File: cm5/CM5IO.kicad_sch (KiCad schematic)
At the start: 11 parts, among them J2 B2B-XH-A_LF__SN_

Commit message: Ordered v2 PCB
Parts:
- J2: value B2B-XH-A_LF__SN_ -> 1x4; symbol dk_Rectangular-Connectors-Headers-Male-Pins:B2B-XH-A_LF__SN_ -> Connector_Generic:Conn_01x04
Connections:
- net +5v: now also J2.1 (Pin_1), J2.4 (Pin_4); no longer J2.2
- net GND: now also J2.2 (Pin_2), J2.3 (Pin_3); no longer J2.1
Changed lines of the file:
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@@
+	)
+	(junction
+		(at 44.45 82.55)
+		(diameter 0)
+		(color 0 0 0 0)
 	)
 	(junction
@@
 		(color 0 0 0 0)
 	)
+	(junction
+		(at 40.64 85.09)
+		(diameter 0)
+		(color 0 0 0 0)
+	)
 	(wire
 		(pts
@@
 	(wire
 		(pts
-			(xy 238.76 86.36) (xy 238.76 161.29)
-		)
-		(stroke
-			(width 0)
-			(type default)
-		)
-	)
-	(wire
-		(pts
-			(xy 153.67 168.91) (xy 232.41 168.91)
-		)
-		(stroke
-			(width 0)
-			(type default)
-		)
-	)
-	(wire
-		(pts
 			(xy 115.57 76.2) (xy 129.54 76.2)
 		)
@@
 	(wire
 		(pts
-			(xy 153.67 168.91) (xy 153.67 157.48)
-		)
-		(stroke
-			(width 0)
-			(type default)
-		)
-	)
-	(wire
-		(pts
-			(xy 50.8 78.74) (xy 50.8 82.55)
-		)
-		(stroke
-			(width 0)
-			(type default)
-		)
-	)
-	(wire
-		(pts
 			(xy 186.69 72.39) (xy 200.66 72.39)
 		)
@@
 	(wire
 		(pts
+			(xy 45.72 85.09) (xy 40.64 85.09)
+		)
+		(stroke
+			(width 0)
+			(type default)
+		)
+	)
+	(wire
+		(pts
 			(xy 204.47 48.26) (xy 214.63 48.26)
 		)
@@
 	(wire
 		(pts
-			(xy 149.86 170.18) (xy 241.3 170.18)
-		)
-		(stroke
-			(width 0)
-			(type default)
-		)
-	)
-	(wire
-		(pts
 			(xy 228.6 166.37) (xy 157.48 166.37)
 		)
@@
 	(wire
 		(pts
-			(xy 53.34 82.55) (xy 53.34 78.74)
+			(xy 44.45 90.17) (xy 45.72 90.17)
 		)
 		(stroke
@@
 	(wire
 		(pts
-			(xy 149.86 157.48) (xy 149.86 170.18)
-		)
-		(stroke
-			(width 0)
-			(type default)
-		)
-	)
-	(wire
-		(pts
 			(xy 162.56 96.52) (xy 162.56 111.76)
 		)
@@
 	(wire
 		(pts
+			(xy 40.64 85.09) (xy 33.02 85.09)
+		)
+		(stroke
+			(width 0)
+			(type default)
+		)
+	)
+	(wire
+		(pts
 			(xy 92.71 101.6) (xy 92.71 104.14)
 		)
@@
 	(wire
 		(pts
+			(xy 44.45 80.01) (xy 44.45 82.55)
+		)
+		(stroke
+			(width 0)
+			(type default)
+		)
+	)
+	(wire
+		(pts
 			(xy 200.66 72.39) (xy 200.66 62.23)
 		)
@@
 	(wire
 		(pts
+			(xy 40.64 87.63) (xy 40.64 85.09)
+		)
+		(stroke
+			(width 0)
+			(type default)
+		)
+	)
+	(wire
+		(pts
 			(xy 129.54 50.8) (xy 120.65 50.8)
 		)
@@
 	(wire
 		(pts
-			(xy 175.26 161.29) (xy 175.26 157.48)
-		)
-		(stroke
-			(width 0)
-			(type default)
-		)
-	)
-	(wire
-		(pts
-			(xy 236.22 160.02) (xy 236.22 86.36)
+			(xy 44.45 82.55) (xy 44.45 90.17)
+		)
+		(stroke
+			(width 0)
+			(type default)
+		)
+	)
+	(wire
+		(pts
+			(xy 45.72 87.63) (xy 40.64 87.63)
 		)
 		(stroke
@@
 	(wire
 		(pts
-			(xy 179.07 157.48) (xy 179.07 160.02)
+			(xy 45.72 82.55) (xy 44.45 82.55)
 		)
 		(stroke
@@
 	(wire
 		(pts
-			(xy 232.41 86.36) (xy 232.41 168.91)
-		)
-		(stroke
-			(width 0)
-			(type default)
-		)
-	)
-	(wire
-		(pts
 			(xy 204.47 22.86) (xy 204.47 48.26)
 		)
@@
 	(wire
 		(pts
-			(xy 179.07 160.02) (xy 236.22 160.02)
-		)
-		(stroke
-			(width 0)
-			(type default)
-		)
-	)
-	(wire
-		(pts
 			(xy 115.57 72.39) (xy 129.54 72.39)
 		)
@@
 		(pts
 			(xy 123.19 22.86) (xy 204.47 22.86)
-		)
-		(stroke
-			(width 0)
-			(type default)
-		)
-	)
-	(wire
-		(pts
-			(xy 241.3 170.18) (xy 241.3 86.36)
-		)
-		(stroke
-			(width 0)
-			(type default)
-		)
-	)
-	(wire
-		(pts
-			(xy 238.76 161.29) (xy 175.26 161.29)
 		)
 		(stroke
@@
 	)
 	(label "+5v"
-		(at 53.34 78.74 0)
+		(at 44.45 80.01 0)
 		(effects
 			(font
@@
 	)
 	(symbol
-		(lib_id "dk_Rectangular-Connectors-Headers-Male-Pins:B2B-XH-A_LF__SN_")
+		(lib_id "Connector_Generic:Conn_01x04")
 		(at 50.8 85.09 0)
 		(unit 1)
@@
 		(fields_autoplaced yes)
 		(property "Reference" "J2"
-			(at 55.88 85.0899 0)
-			(effects
-				(font
-					(size 1.27 1.27)
-				)
-				(justify left)
-			)
-		)
-		(property "Value" "B2B-XH-A_LF__SN_"
-			(at 55.88 87.6299 0)
+			(at 53.34 85.0899 0)
+			(effects
+				(font
+					(size 1.27 1.27)
+				)
+				(justify left)
+			)
+		)
+		(property "Value" "1x4"
+			(at 53.34 87.6299 0)
 			(effects
 				(font
@@
 		)
 		(property "Footprint" "digikey-footprints:PinHeader_1x2_P2.5mm_Drill1.1mm"
-			(at 55.88 80.01 0)
-			(effects
-				(font
-					(size 1.524 1.524)
-				)
-				(justify left)
-				(hide yes)
-			)
-		)
-		(property "Datasheet" "http://www.jst-mfg.com/product/pdf/eng/eXH.pdf"
-			(at 55.88 77.47 0)
-			(effects
-				(font
-					(size 1.524 1.524)
-				)
-				(justify left)
-				(hide yes)
-			)
-		)
-		(property "Description" "CONN HEADER VERT 2POS 2.5MM"
+			(at 50.8 85.09 0)
+			(effects
+				(font
+					(size 1.27 1.27)
+				)
+				(hide yes)
+			)
+		)
+		(property "Datasheet" "~"
+			(at 50.8 85.09 0)
+			(effects
+				(font
+					(size 1.27 1.27)
+				)
+				(hide yes)
+			)
+		)
+		(property "Description" "Generic connector, single row, 01x04, script generated (kicad-library-utils/schlib/autogen/connector/)"
 			(at 50.8 85.09 0)
 			(effects
@@
 		)
 		(pin "1"
+		)
+		(pin "3"
+		)
+		(pin "4"
 		)
 		(instances
@@
 	(symbol
 		(lib_id "power:GND")
-		(at 50.8 78.74 180)
+		(at 33.02 85.09 180)
 		(unit 1)
 		(exclude_from_sim no)
@@
 		(dnp no)
 		(property "Reference" "#PWR063"
-			(at 50.8 72.39 0)
+			(at 33.02 78.74 0)
 			(effects
 				(font
@@
 		)
 		(property "Value" "GND"
-			(at 50.673 74.3458 0)
+			(at 32.893 80.6958 0)
 			(effects
 				(font
@@
 		)
 		(property "Footprint" ""
-			(at 50.8 78.74 0)
+			(at 33.02 85.09 0)
 			(effects
 				(font
@@
 		)
 		(property "Datasheet" ""
-			(at 50.8 78.74 0)
+			(at 33.02 85.09 0)
 			(effects
 				(font
@@
 		)
 		(property "Description" "Power symbol creates a global label with name \"GND\" , ground"
-			(at 50.8 78.74 0)
-			(effects
-				(font
+			(at 33.02 85.09 0)
+			(effects
+				(font

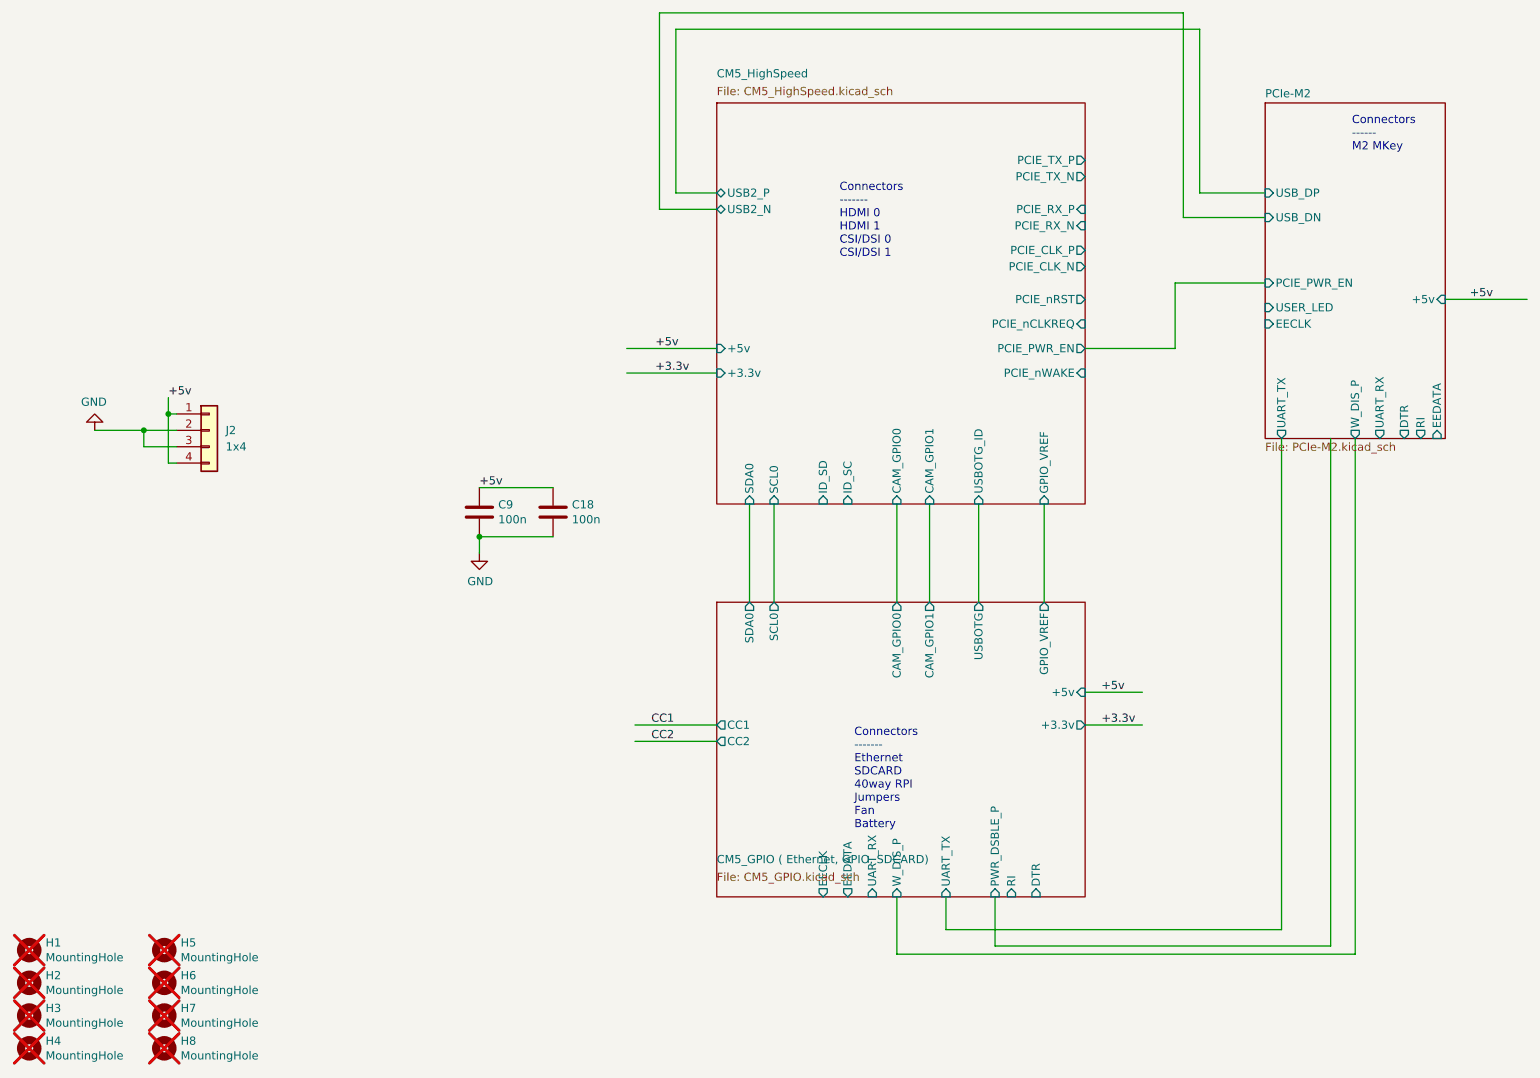
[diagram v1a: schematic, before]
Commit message: PCM1863 switchover (#5)
* Oops, basically brand new ADC design using a new chip

* Working PCB and working driver, sort of

* --amend
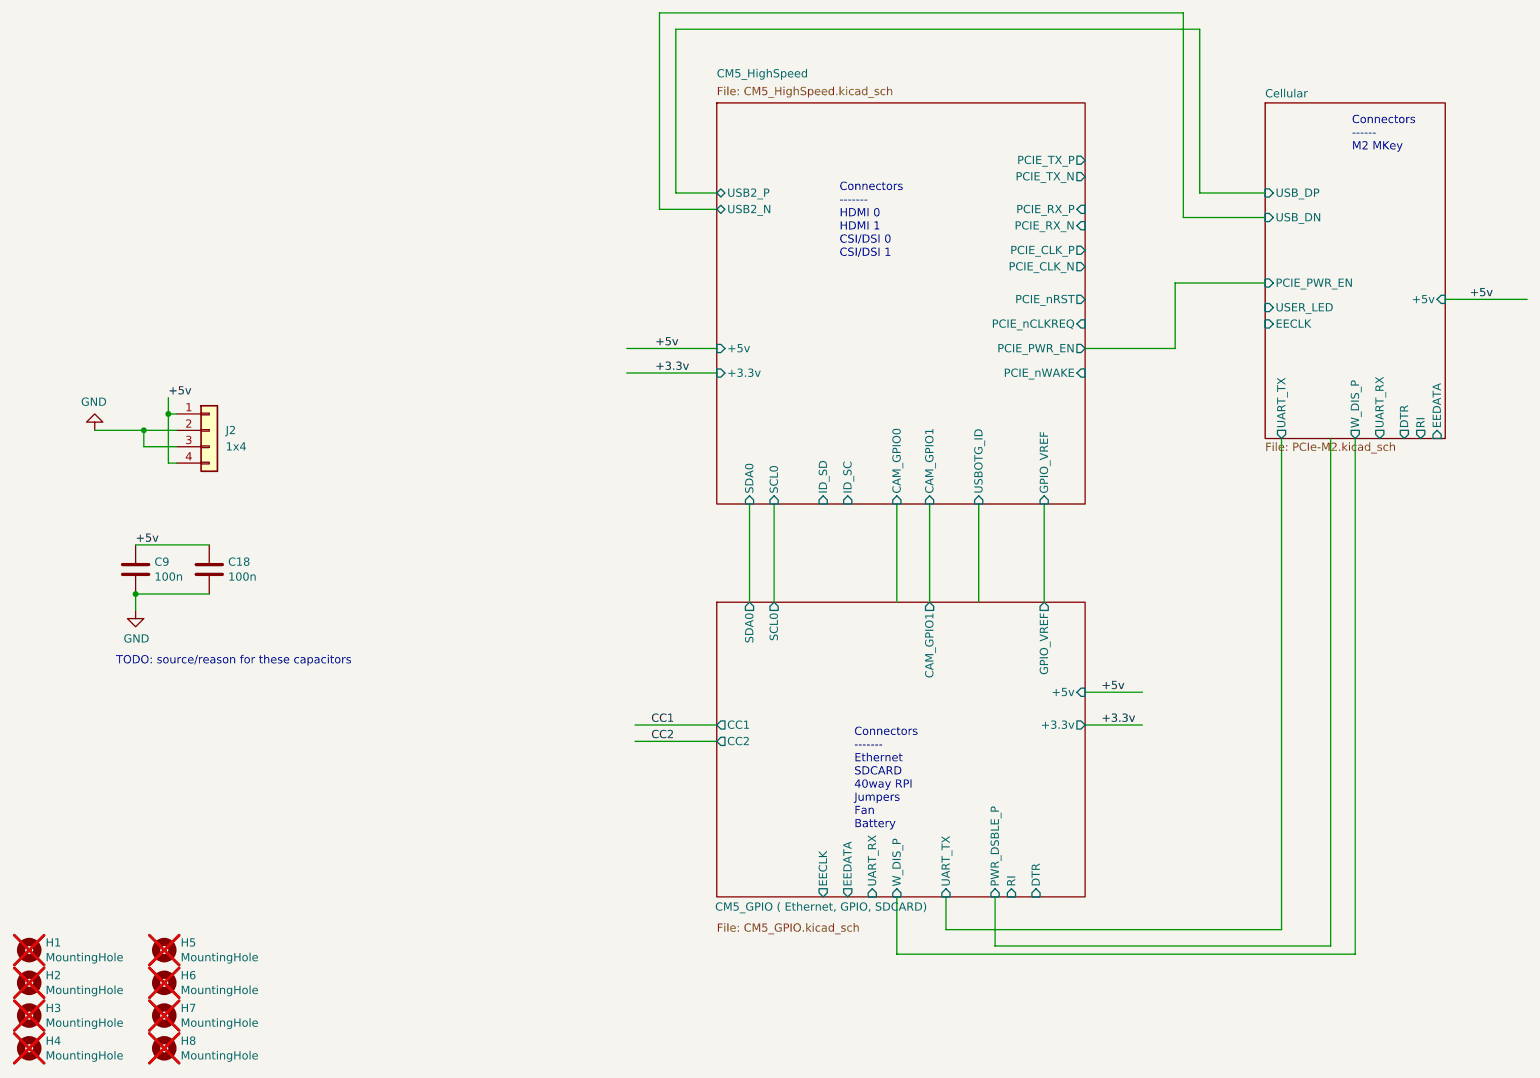
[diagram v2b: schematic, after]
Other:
- sheet PCIe-M2 renamed Cellular
- sheet CM5_GPIO ( Ethernet, GPIO, SDCARD) ports: added none; removed CAM_GPIO0, USBOTG
- note added: "TODO: source/reason for these capacitors"
- moved on the sheet: C18, C9
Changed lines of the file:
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@@
+		)
+	)
+	(text "TODO: source/reason for these capacitors"
+		(exclude_from_sim no)
+		(at 54.61 120.904 0)
+		(effects
+			(font
+				(size 1.27 1.27)
+			)
 		)
 	)
@@
 	)
 	(junction
-		(at 92.71 101.6)
+		(at 39.37 110.49)
 		(diameter 0)
 		(color 0 0 0 0)
@@
 	(wire
 		(pts
-			(xy 92.71 101.6) (xy 104.14 101.6)
+			(xy 39.37 110.49) (xy 50.8 110.49)
 		)
 		(stroke
@@
 	(wire
 		(pts
-			(xy 92.71 101.6) (xy 92.71 104.14)
+			(xy 39.37 110.49) (xy 39.37 113.03)
 		)
 		(stroke
@@
 	(wire
 		(pts
-			(xy 92.71 93.98) (xy 104.14 93.98)
+			(xy 39.37 102.87) (xy 50.8 102.87)
 		)
 		(stroke
@@
 	)
 	(label "+5v"
-		(at 92.71 93.98 0)
+		(at 39.37 102.87 0)
 		(effects
 			(font
@@
 	(symbol
 		(lib_id "Device:C")
-		(at 104.14 97.79 0)
+		(at 50.8 106.68 0)
 		(unit 1)
 		(exclude_from_sim no)
@@
 		(dnp no)
 		(property "Reference" "C18"
-			(at 107.061 96.6216 0)
+			(at 53.721 105.5116 0)
 			(effects
 				(font
@@
 		)
 		(property "Value" "100n"
-			(at 107.061 98.933 0)
+			(at 53.721 107.823 0)
 			(effects
 				(font
@@
 		)
 		(property "Footprint" "Capacitor_SMD:C_0402_1005Metric"
-			(at 105.1052 101.6 0)
+			(at 51.7652 110.49 0)
 			(effects
 				(font
@@
 		)
 		(property "Datasheet" "https://search.murata.co.jp/Ceramy/image/img/A01X/G101/ENG/GRM155R71C104KA88-01.pdf"
-			(at 104.14 97.79 0)
+			(at 50.8 106.68 0)
 			(effects
 				(font
@@
 		)
 		(property "Description" ""
-			(at 104.14 97.79 0)
+			(at 50.8 106.68 0)
 			(effects
 				(font
@@
 		)
 		(property "Field4" "Farnell"
-			(at 104.14 97.79 0)
+			(at 50.8 106.68 0)
 			(effects
 				(font
@@
 		)
 		(property "Field5" "2611911"
-			(at 104.14 97.79 0)
+			(at 50.8 106.68 0)
 			(effects
 				(font
@@
 		)
 		(property "Field6" "RM EMK105 B7104KV-F"
-			(at 104.14 97.79 0)
+			(at 50.8 106.68 0)
 			(effects
 				(font
@@
 		)
 		(property "Field7" "TAIYO YUDEN EUROPE GMBH"
-			(at 104.14 97.79 0)
+			(at 50.8 106.68 0)
 			(effects
 				(font
@@
 		)
 		(property "Field8" "110091611"
-			(at 104.14 97.79 0)
+			(at 50.8 106.68 0)
 			(effects
 				(font
@@
 		)
 		(property "Part Description" "	0.1uF 10% 16V Ceramic Capacitor X7R 0402 (1005 Metric)"
-			(at 104.14 97.79 0)
+			(at 50.8 106.68 0)
 			(effects
 				(font
@@
 		)
 		(property "LCSC" "C327024"
-			(at 104.14 97.79 0)
+			(at 50.8 106.68 0)
 			(effects
 				(font
@@
 	(symbol
 		(lib_id "Device:C")
-		(at 92.71 97.79 0)
+		(at 39.37 106.68 0)
 		(unit 1)
 		(exclude_from_sim no)
@@
 		(dnp no)
 		(property "Reference" "C9"
-			(at 95.631 96.6216 0)
+			(at 42.291 105.5116 0)
 			(effects
 				(font
@@
 		)
 		(property "Value" "100n"
-			(at 95.631 98.933 0)
+			(at 42.291 107.823 0)
 			(effects
 				(font
@@
 		)
 		(property "Footprint" "Capacitor_SMD:C_0402_1005Metric"
-			(at 93.6752 101.6 0)
+			(at 40.3352 110.49 0)
 			(effects
 				(font
@@
 		)
 		(property "Datasheet" "https://search.murata.co.jp/Ceramy/image/img/A01X/G101/ENG/GRM155R71C104KA88-01.pdf"
-			(at 92.71 97.79 0)
+			(at 39.37 106.68 0)
 			(effects
 				(font
@@
 		)
 		(property "Description" ""
-			(at 92.71 97.79 0)
+			(at 39.37 106.68 0)
 			(effects
 				(font
@@
 		)
 		(property "Field4" "Farnell"
-			(at 92.71 97.79 0)
+			(at 39.37 106.68 0)
 			(effects
 				(font
@@
 		)
 		(property "Field5" "2611911"
-			(at 92.71 97.79 0)
+			(at 39.37 106.68 0)
 			(effects
 				(font
@@
 		)
 		(property "Field6" "RM EMK105 B7104KV-F"
-			(at 92.71 97.79 0)
+			(at 39.37 106.68 0)
 			(effects
 				(font
@@
 		)
 		(property "Field7" "TAIYO YUDEN EUROPE GMBH"
-			(at 92.71 97.79 0)
+			(at 39.37 106.68 0)
 			(effects
 				(font
@@
 		)
 		(property "Field8" "110091611"
-			(at 92.71 97.79 0)
+			(at 39.37 106.68 0)
 			(effects
 				(font
@@
 		)
 		(property "Part Description" "	0.1uF 10% 16V Ceramic Capacitor X7R 0402 (1005 Metric)"
-			(at 92.71 97.79 0)
+			(at 39.37 106.68 0)
 			(effects
 				(font
@@
 		)
 		(property "LCSC" "C327024"
-			(at 92.71 97.79 0)
+			(at 39.37 106.68 0)
 			(effects
 				(font
@@
 	(symbol
 		(lib_id "power:GND")
-		(at 92.71 104.14 0)
+		(at 39.37 113.03 0)
 		(unit 1)
 		(exclude_from_sim no)
@@
 		(dnp no)
 		(property "Reference" "#PWR013"
-			(at 92.71 110.49 0)
+			(at 39.37 119.38 0)
 			(effects
 				(font
@@
 		)
 		(property "Value" "GND"
-			(at 92.837 108.5342 0)
+			(at 39.497 117.4242 0)
 			(effects
 				(font
@@
 		)
 		(property "Footprint" ""
-			(at 92.71 104.14 0)
+			(at 39.37 113.03 0)
 			(effects
 				(font
@@
 		)
 		(property "Datasheet" ""
-			(at 92.71 104.14 0)
+			(at 39.37 113.03 0)
 			(effects
 				(font
@@
 		)
 		(property "Description" "Power symbol creates a global label with name \"GND\" , ground"
-			(at 92.71 104.14 0)
+			(at 39.37 113.03 0)
 			(effects
 				(font
@@
 		)
 		(property "Sheetname" "CM5_GPIO ( Ethernet, GPIO, SDCARD)"
-			(at 129.54 152.4 0)
+			(at 129.286 159.766 0)
 			(effects
 				(font
@@
 		)
 		(property "Sheetfile" "CM5_GPIO.kicad_sch"
-			(at 129.54 153.67 0)
+			(at 129.54 161.544 0)
 			(effects
 				(font
@@
 			)
 		)
-		(pin "CAM_GPIO0" output
-			(at 157.48 111.76 90)
-			(effects
-				(font
-					(size 1.27 1.27)
-				)
-				(justify right)
-			)
-		)
 		(pin "CAM_GPIO1" output
 			(at 162.56 111.76 90)
@@
 				)
 				(justify left)
-			)
-		)
-		(pin "USBOTG" output
-			(at 170.18 111.76 90)
-			(effects
-				(font
-					(size 1.27 1.27)
-				)
-				(justify right)
 			)
 		)
@@
 			(color 255 255 255 0.0000)
 		)
-		(property "Sheetname" "PCIe-M2"
+		(property "Sheetname" "Cellular"
 			(at 214.63 33.5786 0)
 			(effects
